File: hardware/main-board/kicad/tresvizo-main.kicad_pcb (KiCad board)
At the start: 4 copper layers, 46 x 64 mm, 114 parts, among them J101 PANEL_USB, J102 BATTERY, J301 GNSS, J401 TF-015, J402 BOTON, J403 OLED, J404 NTC, J405 IMU, Q101 AO3400A, Q102 AO3401A, Q103 AO3400A, Q401 AO3401A, Q402 AO3400A, SW201 RESET, SW202 BOOT, U101 USBLC6-2SC6, U102 BQ25798RQMR, U103 MAX17048G+T10, U105 TPS62903RPJR, U201 ESP32-S3-WROOM-1-N16R2, U301 TPS63070RNMR, U302 USBLC6-2SC6, U303 USBLC6-2SC6

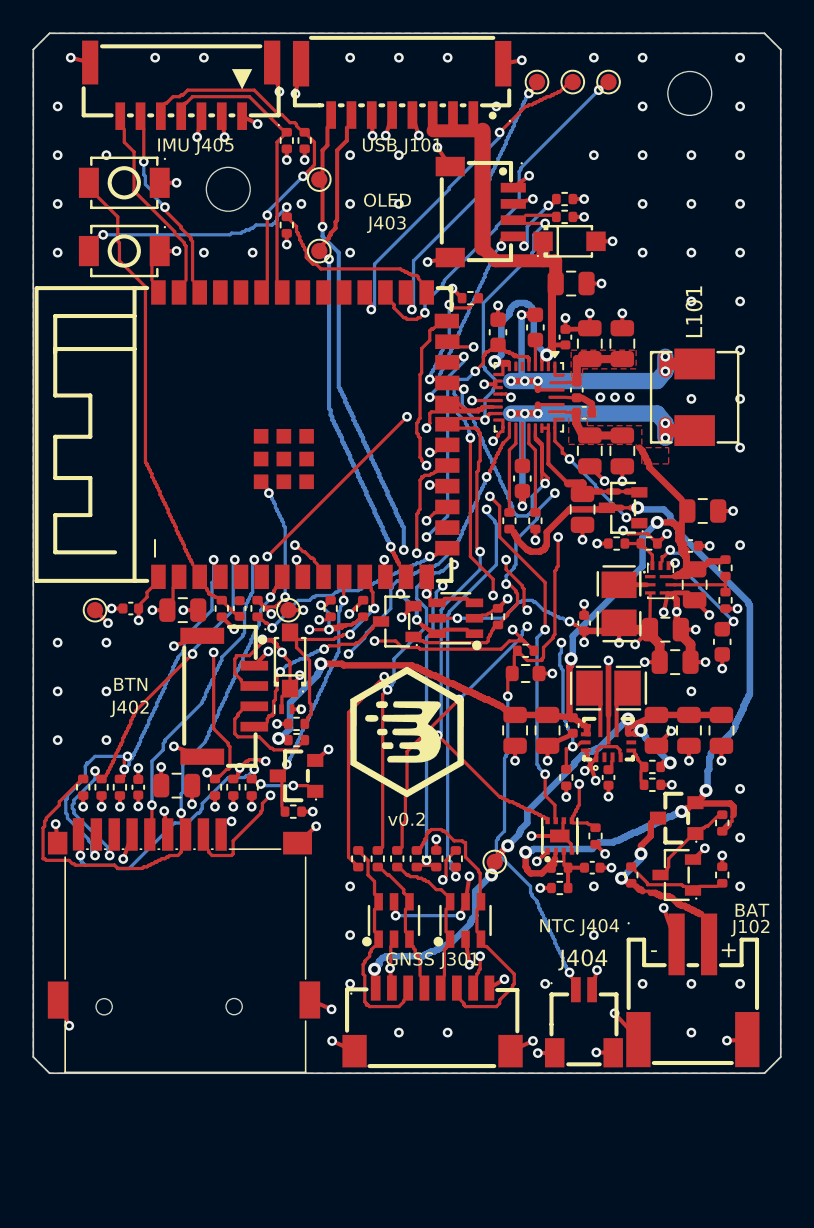
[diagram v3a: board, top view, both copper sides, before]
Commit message: Placa principal v0.3 compacta: 36 × 71.5 mm para el tubo de Ø52, con USB-C, OLED, botón, LED y BMI088 en la placa
- Rama exploratoria pedida por el propietario el 07-10-2026. Especificación, interfaces con la
  carcasa, colocación y auditoría en research/v03-compacta.md.
- Esquema (ERC 0):
  - USB-C TYPE-C-31-M-12 con Rd de 5.1k, TVS SMF15A y USBLC6;
  - pulsador TS-1187A a BTN_N;
  - LED de estado en GPIO48 con 330 Ω;
  - OLED del propietario soldada sobre pads SMD (J403);
  - BMI088 por I2C (GPIO41/42, INT1 en GPIO2 e INT3 en GPIO1);
  - J102 en GH 4, con dos contactos por polo;
  - TP208 y TP209 en la UART0.
  Fuera J402, J405 y Q402; la panel-usb ya no se usa.
- Placa de 4 capas con muescas para la funda del USB-C y para la clavija SMA de la carrier.
  - Los bloques del cargador y de los reguladores se mueven sin cambiar su geometría interna.
  - La antena del WROOM va hacia −X, con zona sin cobre.
  - Panel de una sola placa.
  - DRC con 0 violaciones, 0 sin conectar y 0 de paridad; el panel, igual.
- Auditoría eléctrica independiente (08-10-2026), con sus siete puntos corregidos:
  - las soldaduras de la OLED ya no quedan frente al SMA de la carrier;
  - puentes del panel lejos del IMU y de los condensadores de potencia;
  - zona sin cobre de la antena más grande;
  - GND de J102 y vías dobles en VPACK;
  - vías junto al pad de tierra del WROOM;
  - LED más brillante;
  - pads de la UART.
- cad/export_board_step.py exporta el STEP en los ejes de la carcasa, con los modelos de LCSC
  corregidos. cad/check_heights.py comprueba los altos contra el tubo: todas las piezas caben con
  0.3 mm de aire.
- Cambios en los scripts:
  - route_rest.py admite límites de búsqueda por entorno;
  - fanout.py respeta las vías prerruteadas;
  - finish_pcb.py --final quita las vías sin uso;
  - cost_jlc.py sirve para una sola placa.
- Costo estimado en JLCPCB: 236.43 USD por 5 placas montadas, sin el PCB ni el envío.
- El build casi siempre se repite igual. En una de cuatro corrid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
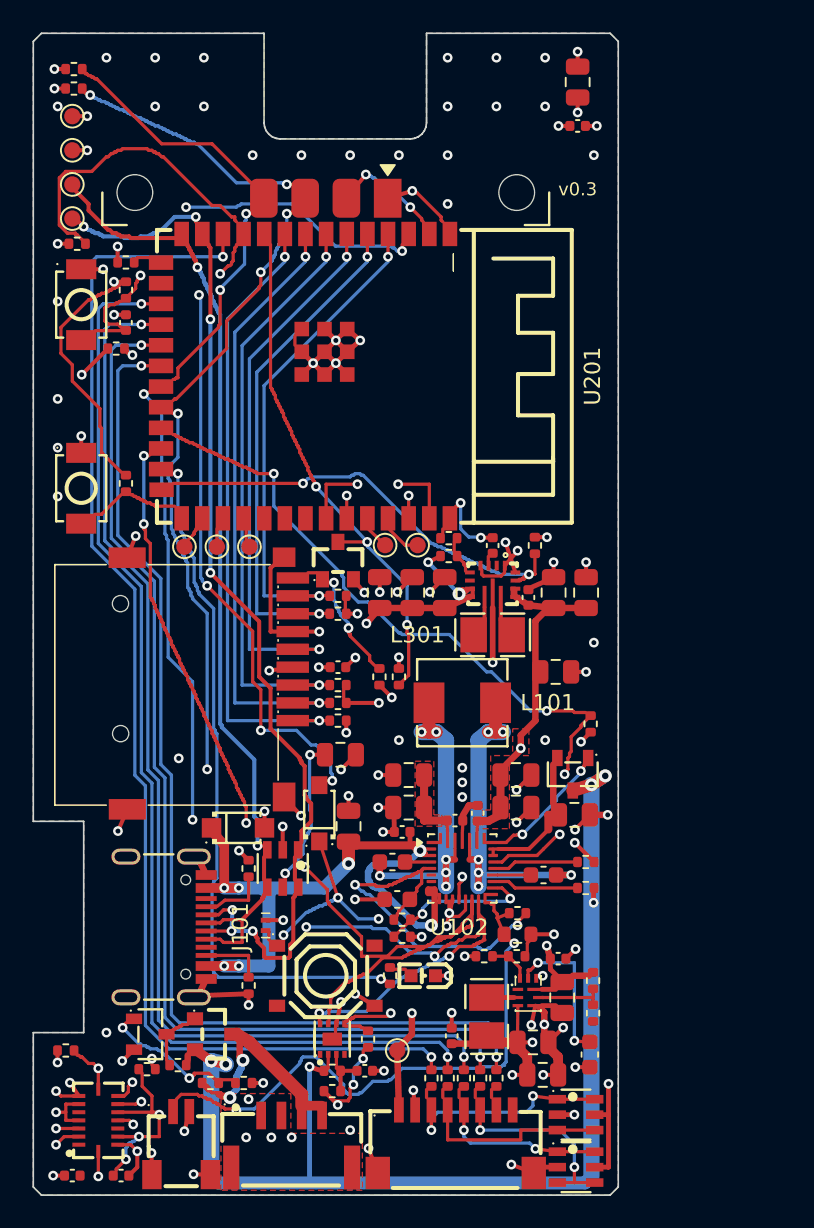
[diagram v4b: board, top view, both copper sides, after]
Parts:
- removed H1, H2: MountingHole_2.7mm, MountingHole_2.7mm
- removed J402: BOTON, tresvizo_lcsc:CONN-SMD_4P-P1.25_SM04B-GHS-TB-LF-SN
- removed J405: IMU, tresvizo_lcsc:CONN-SMD_SM7B-GHS-TB-LF-SN
- removed Q402: AO3400A, tresvizo_lcsc:SOT-23-3_L2.9-W1.3-P1.90-LS2.4-BR
- removed R410: 100k, Resistor_SMD:R_0402_1005Metric
- added C403: 100nF, Capacitor_SMD:C_0402_1005Metric, F.Cu at (102.4, 170.3)
- added C404: 100nF, Capacitor_SMD:C_0402_1005Metric, F.Cu at (105.4, 170.3)
- added D403: KT-0603R, tresvizo_lcsc:LED-SMD_L1.6-W0.8-R-RD, F.Cu at (124.0, 158.0)
- added R119: 5.1k, Resistor_SMD:R_0402_1005Metric, F.Cu at (113.2, 151.4)
- added R120: 5.1k, Resistor_SMD:R_0402_1005Metric, F.Cu at (113.2, 158.6)
- added SW401: BOTON, tresvizo_lcsc:SW-SMD_4P-L5.1-W5.1-P3.70-LS6.5-TL_H1.5, F.Cu at (118.0, 158.0)
- added TP208: U0TXD, TestPoint:TestPoint_Pad_D1.0mm, F.Cu at (123.7, 131.5)
- added TP209: U0RXD, TestPoint:TestPoint_Pad_D1.0mm, F.Cu at (121.7, 131.5)
- added U401: BMI088, tresvizo_lcsc:LGA-16_L4.5-W3.0-P0.50-BL, F.Cu at (104.0, 166.9)
- J101: value PANEL_USB -> USB_C; footprint tresvizo_lcsc:CONN-SMD_8P-P1.25_XUNPU-WAFER-GH1.25-8PWB -> tresvizo_lcsc:USB-C_SMD-TYPE-C-31-M-12
- J102: footprint tresvizo_lcsc:CONN-SMD_P2.00_S2B-PH-SM4-TB-LF-SN -> tresvizo_lcsc:CONN-SMD_4P-P1.25_SM04B-GHS-TB-LF-SN
- J403: footprint tresvizo_lcsc:CONN-SMD_4P-P1.00_SM04B-SRSS-TB-LF-SN -> tresvizo_lcsc:OLED_0.96in_I2C_4P_P2.54mm
- R409: value 100 -> 330
- moved R412 57.9 mm to (102.0, 162.6), turned to 0 degrees
- moved R411 57.8 mm to (107.0, 163.8), turned to 0 degrees
- moved J101 53.6 mm to (108.2, 155.0), turned to -90 degrees
- moved D101 41.5 mm to (112.6, 148.9)
- moved C201 40.6 mm to (133.5, 103.0), turned to 90 degrees
- moved C202 40.5 mm to (133.5, 105.7)
- moved TP204 37.4 mm to (111.3, 131.6)
- moved R308 37.1 mm to (105.1, 119.4), turned to 180 degrees
- moved R109 36.7 mm to (108.9, 163.5), turned to 180 degrees
- moved C104 36.1 mm to (119.4, 148.8), turned to 90 degrees
- moved TP203 35.9 mm to (109.3, 131.6)
- moved C103 35.4 mm to (122.4, 153.3), turned to 180 degrees
- moved TP205 34.8 mm to (113.3, 131.6)
- moved C101 34.1 mm to (122.1, 151.0), turned to 180 degrees
- moved Q103 33.8 mm to (107.2, 161.6), turned to 180 degrees
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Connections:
- net /microSD, IMU por conector y panel/SD_CD_N renamed /microSD, IMU, OLED, botón y LED/SD_CD_N
- J102 pad 2: /Alimentación, carga y batería/VBATT_IN -> GND
- J403 pad 3: I2C_SDA -> I2C_SCL
- J403 pad 4: I2C_SCL -> I2C_SDA
- R409 pad 1: VSYS -> LED_STATUS
- R409 pad 2: /microSD, IMU por conector y panel/BTN_LED_A -> /microSD, IMU, OLED, botón y LED/LED_STATUS_A
- U201 pad 25: BTN_LED_EN -> LED_STATUS
- U201 pad 36: unconnected-(U201-RXD0-Pad36) -> /ESP32-S3/ESP_RXD0
- U201 pad 37: unconnected-(U201-TXD0-Pad37) -> /ESP32-S3/ESP_TXD0
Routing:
- net GNSS_TX_MCU: track 20.1 -> 77.2 mm
- net IMU_INT1: track 10.5 -> 63.1 mm
- net IMU_INT3: track 10.9 -> 59.1 mm, vias 0 -> 2
- net BTN_SENSE_N: track 12.3 -> 57.6 mm, vias 2 -> 5
- net GNSS_TXD2_MCU: track 24.5 -> 69.4 mm, vias 3 -> 2
- net I2C_SDA: track 50.6 -> 93.7 mm, vias 4 -> 8
- net LED_STATUS: track 0.00 -> 43.0 mm, vias 0 -> 2
- net GNSS_EVENT_MCU: track 26.8 -> 69.1 mm
- net GNSS_PPS_MCU: track 29.0 -> 68.5 mm, vias 5 -> 2
- net IMU_SDA: track 16.1 -> 55.1 mm, vias 0 -> 3
- net +3V3: track 48.9 -> 87.5 mm, vias 35 -> 34
- net I2C_SCL: track 55.0 -> 92.0 mm, vias 8 -> 7
- net GNSS_RESET_MCU: track 30.1 -> 66.6 mm, vias 3 -> 2
- net IMU_SCL: track 20.0 -> 52.1 mm
- net BTN_LED_EN: track 28.8 -> 0.00 mm, vias 3 -> 0
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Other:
- board size 46 x 64 mm -> 36 x 71.5 mm
- board text added: "1-2 BAT- 3-4 BAT+"
- board text added: "2S: R103=8.2k R116=3.9k U103=MAX17049"
- board text added: "2S: R112 NC R114 0R"
- board text added: "BAT J102"
- board text added: "TresVizo MeridianV - placa principal v0.3"
- board text added: "v0.3"
- board text removed: "+"
- board text removed: "-"
- board text removed: "2S: R103=8.2k R116=3.9k U103=MAX17049 R112 NC R114 0R"
- board text removed: "BAT"
- board text removed: "BTN"
- board text removed: "IMU J405"
- board text removed: "J102"
- board text removed: "J402"
- board text removed: "J403"
- board text removed: "OLED"
- board text removed: "TresVizo MeridianV - placa principal v0.2"
- board text removed: "USB J101"
- board text removed: "v0.2"

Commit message: v0.3: endurecimiento de la placa y de la carcasa V3.0 (Ø56 × 111)
Carcasa V3.0:
- Tubo de Ø56 × 111 con pared de 2.4 (antes Ø52 × 100). Holguras, en la posición final y en los
  11 barridos de montaje:
  - 0.4 mm en los ajustes entre piezas impresas;
  - 0.25 por cara en los rieles de la placa;
  - 0.5 de aire a todo lo comprado.
  El coaxial va con curvas de R 10. La placa no cambió de sitio; la carrier va 0.1 más atrás.
- Antena:
  - SMA hembra de panel al centro de la tapa para la HA-901A. La tienda da conector macho
    («SMA-J»); si resulta hembra, un parámetro cambia la tapa a un paso de 12 mm.
  - Coaxial RG 178 B/U de unos 75 mm, con SMA macho acodado en la carrier.
  - Arandelas ISO 7092 en los tornillos de la antena.
- Correcciones de la revisión externa:
  - eje real de la tarjeta microSD (z 40.9), tomado de J401 y no de la ranura;
  - arnés real de la batería y la NTC, con su recorrido;
  - procedimiento de desarmado completo.
- Tapa de TPU amarrada para el USB-C y la microSD, logo en relieve de 0.5 al frente y líneas
  verticales decorativas atrás, como en V2.3.
- check_v3_0.py: 0 choques y guarda de pared sin faltantes. Se cumplen los objetivos de holgura; la
  pared más delgada mide 1.198 mm, en una unión.

Placa v0.3, sin mover piezas:
- C104, C106 y C107 pasan de 22 a 10 µF (C15850). La carga que pide el USB al enchufar baja de unos
  259 a 118 µC. Sigue arriba de la regla de 10 µF de USB 2.0: queda como decisión del propietario.
- VSYS por In2.Cu a 1.2 mm y GNSS_5V a 0.6 mm, con más vías.
- Tabla de valores para el firmware: ICHG de 1.5 A como máximo, límite de entrada, reinicio con el
  botón, OLED girada 180° y ejes del IMU.
- ERC 0. DRC 0/0/0 y panel 0/0. Dos builds iguales byte a byte. 234.15 USD por 5 placas montadas.
- check_heights.py lee el tubo de la carcasa y mide 0.5 de aire en radio: todas las piezas caben.

Pendiente: confirmar el conector de la antena, medir la carrier y la OLED, y el orden de los pines
de la OLED.
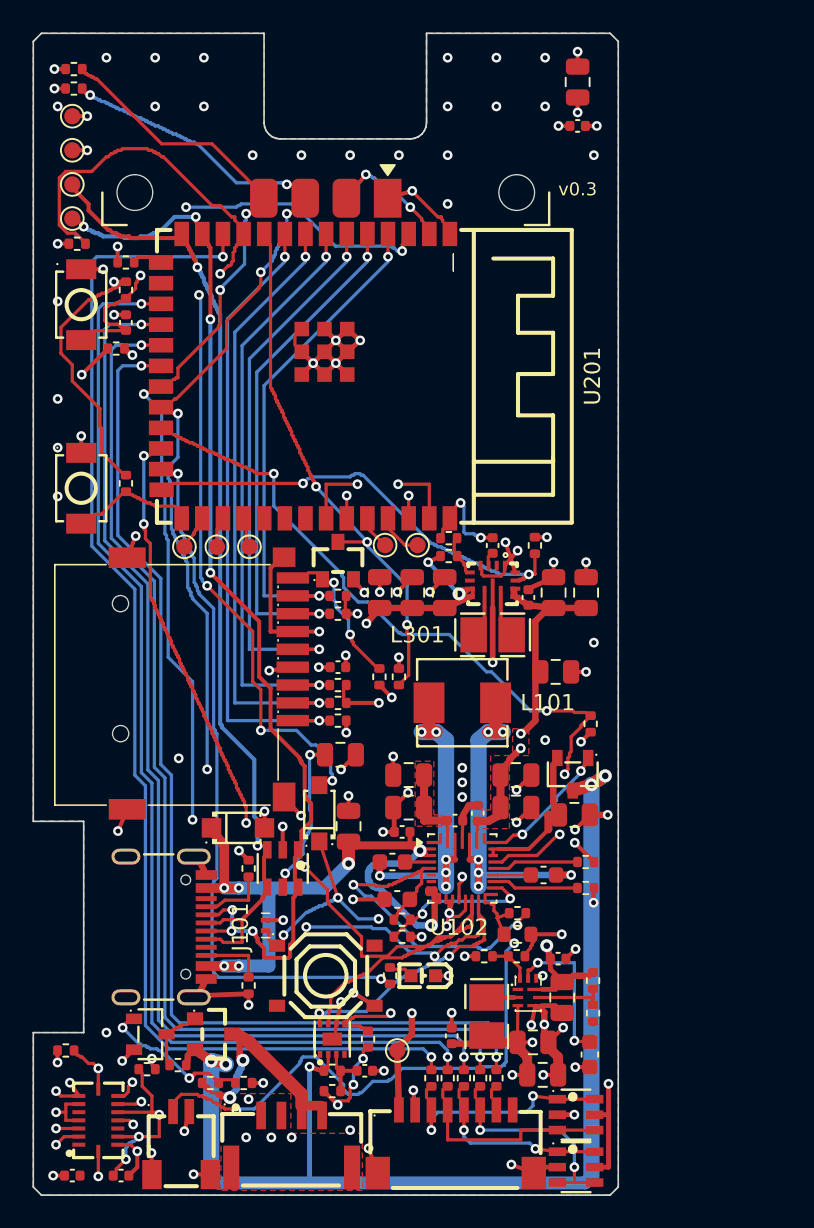
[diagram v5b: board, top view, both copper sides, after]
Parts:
- C104, C106, C107: value 22uF -> 10uF
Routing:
- net GND: track 133.0 -> 134.6 mm, vias 112 -> 111
- net VSYS: track 36.5 -> 36.6 mm, vias 2 -> 3
